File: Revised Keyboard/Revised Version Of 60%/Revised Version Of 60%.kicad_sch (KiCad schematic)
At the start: 104 parts, among them J1 AVR-ISP-6, SW1 SW_Push, U1 AT90USB1286-A, U2 PRTR5V0U2X, Y1 Crystal_GND24_Small

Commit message: Updated PCB
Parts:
- removed R1, R2: 22, Resistor_SMD:R_0805_2012Metric_Pad1.20x1.40mm_HandSolder, symbol Device:R_Small
- MX_CAPS1: footprint MX_Alps_Hybrid:MX-1U-NoLED -> MX_Alps_Hybrid:MX-1.25U-NoLED
- renumbered D1 to D_?1, D2 to D_Enter1, MX_1 to MX_?1
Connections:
- net D+: now also U1.5 (D+); no longer U2.4 (VCC)
- net D-: now also U1.4 (D-)
- net GND: now also U2.1 (GND); no longer U2.3 (IO2)
- net VCC: now also U2.4 (VCC); no longer U2.2 (IO1)
- net DN: now reaches R7.1, USB1.5 (DN2), USB1.7 (DN1)
- net DN: now also U2.3 (IO2); no longer U2.1 (GND)
- net DP: now reaches R8.2, USB1.6 (DP1), USB1.8 (DP2)
- net DP: now also U2.2 (IO1)
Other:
- moved on the sheet: U2

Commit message: Update
General Update of files
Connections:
- net MISO: now also U1.45 (PA6); no longer U1.49 (PA2)
- net MOSI: now also U1.46 (PA5); no longer U1.50 (PA1)
- net SCK: now also U1.47 (PA4); no longer U1.51 (PA0)
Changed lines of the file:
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@@
-    (stroke (width 0) (type default) (color 0 0 0 0))
-  )
-  (wire (pts (xy 121.92 58.42) (xy 128.27 58.42))
     (stroke (width 0) (type default) (color 0 0 0 0))
   )
@@
     (stroke (width 0) (type default) (color 0 0 0 0))
   )
-  (wire (pts (xy 121.92 55.88) (xy 128.27 55.88))
-    (stroke (width 0) (type default) (color 0 0 0 0))
-  )
   (wire (pts (xy 233.68 85.09) (xy 240.03 85.09))
     (stroke (width 0) (type default) (color 0 0 0 0))
@@
     (stroke (width 0) (type default) (color 0 0 0 0))
   )
-  (wire (pts (xy 121.92 53.34) (xy 128.27 53.34))
-    (stroke (width 0) (type default) (color 0 0 0 0))
-  )
   (wire (pts (xy 252.73 90.17) (xy 254 90.17))
     (stroke (width 0) (type default) (color 0 0 0 0))
@@
     (stroke (width 0) (type default) (color 0 0 0 0))
   )
-  (global_label "MOSI" (shape input) (at 128.27 55.88 0) (fields_autoplaced)
+  (global_label "MOSI" (shape input) (at 121.92 66.04 0) (fields_autoplaced)
     (effects (font (size 1.27 1.27)) (justify left))
-    (property "Intersheet References" "${INTERSHEET_REFS}" (id 0) (at 135.2793 55.9594 0)
+    (property "Intersheet References" "${INTERSHEET_REFS}" (id 0) (at 128.9293 66.1194 0)
       (effects (font (size 1.27 1.27)) (justify left) hide)
     )
@@
     )
   )
-  (global_label "SCK" (shape input) (at 128.27 53.34 0) (fields_autoplaced)
+  (global_label "SCK" (shape input) (at 121.92 63.5 0) (fields_autoplaced)
     (effects (font (size 1.27 1.27)) (justify left))
-    (property "Intersheet References" "${INTERSHEET_REFS}" (id 0) (at 134.4326 53.4194 0)
+    (property "Intersheet References" "${INTERSHEET_REFS}" (id 0) (at 128.0826 63.5794 0)
       (effects (font (size 1.27 1.27)) (justify left) hide)
     )
@@
     )
   )
-  (global_label "MISO" (shape input) (at 128.27 58.42 0) (fields_autoplaced)
+  (global_label "MISO" (shape input) (at 121.92 68.58 0) (fields_autoplaced)
     (effects (font (size 1.27 1.27)) (justify left))
-    (property "Intersheet References" "${INTERSHEET_REFS}" (id 0) (at 135.2793 58.4994 0)
+    (property "Intersheet References" "${INTERSHEET_REFS}" (id 0) (at 128.9293 68.6594 0)
       (effects (font (size 1.27 1.27)) (justify left) hide)
     )

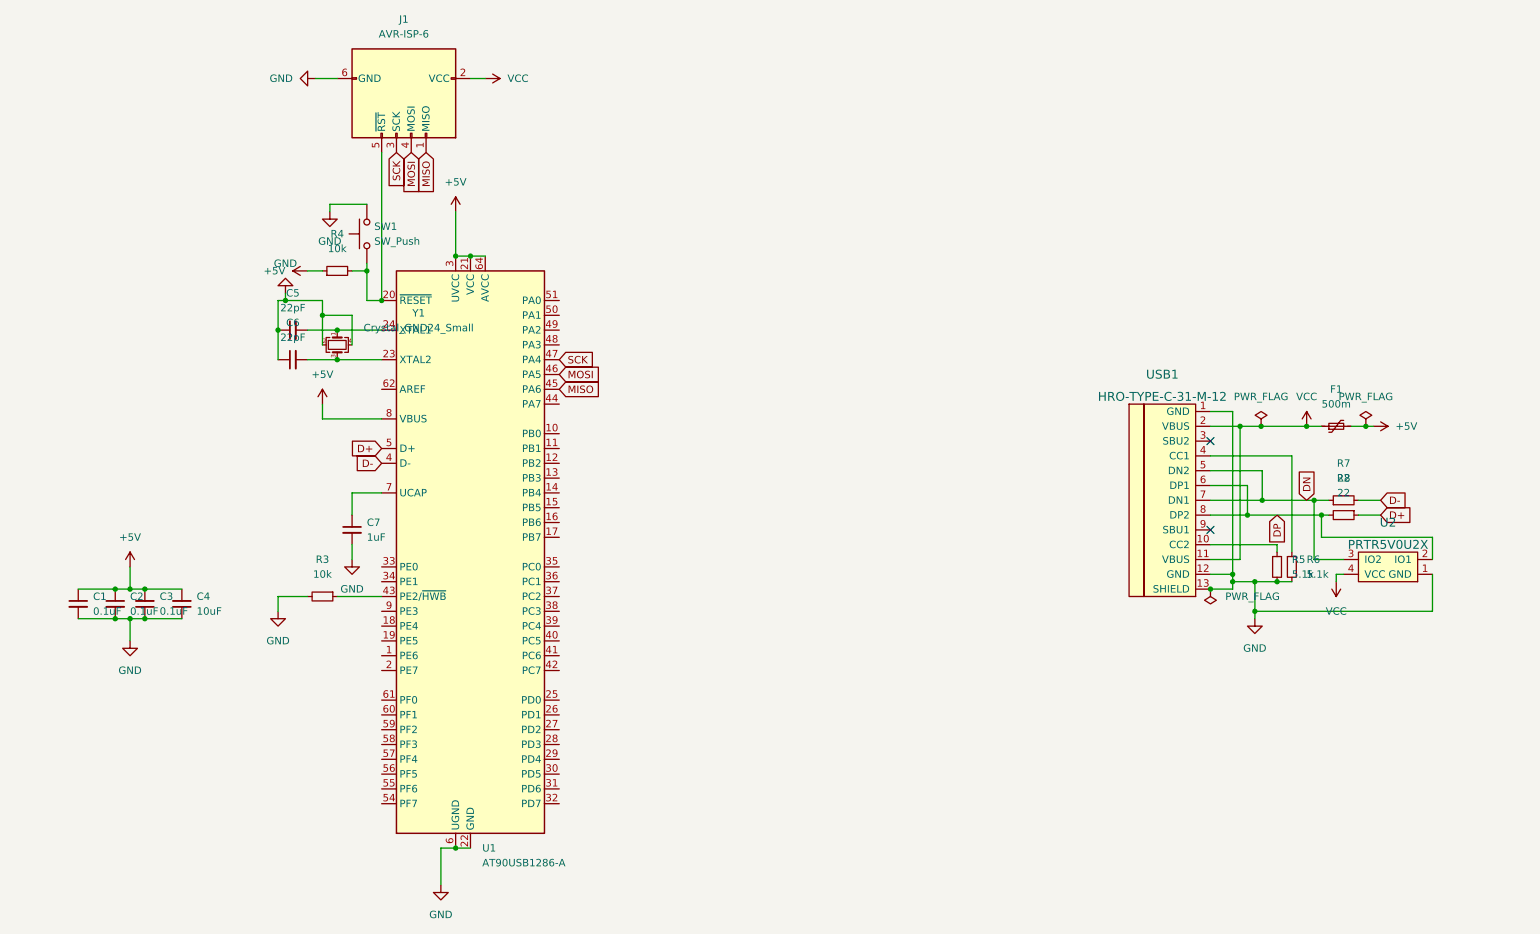
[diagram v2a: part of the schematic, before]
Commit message: Keyboard Update
Changed to a smaller microcontroller
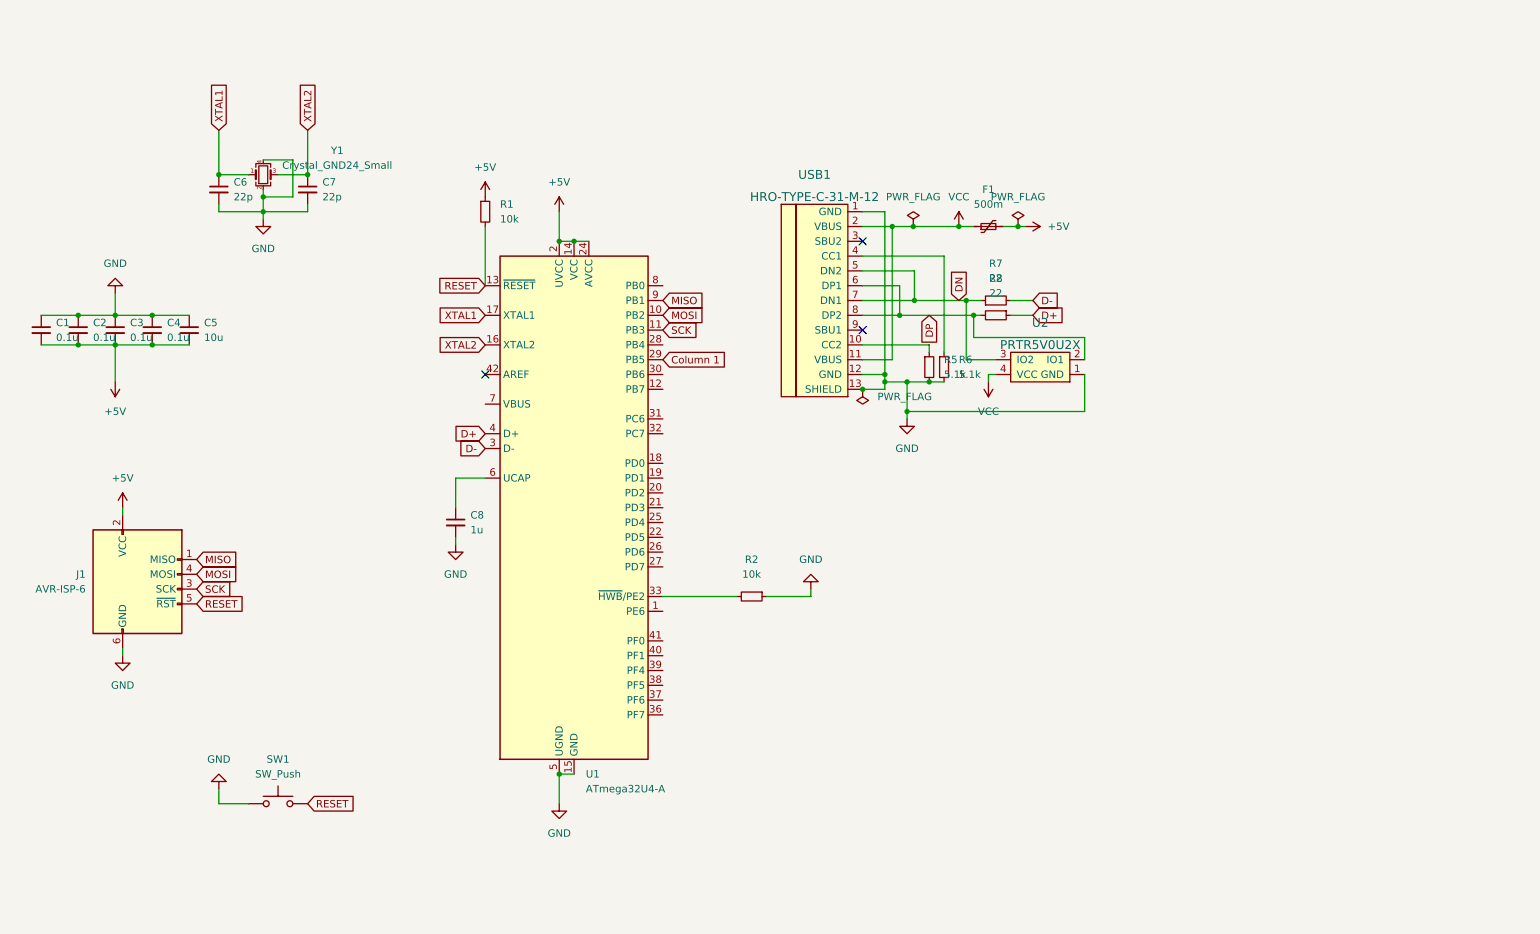
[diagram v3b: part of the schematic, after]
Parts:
- removed R3, R4: 10k, Resistor_SMD:R_0805_2012Metric_Pad1.20x1.40mm_HandSolder, symbol Device:R_Small
- removed U1: AT90USB1286-A, Package_QFP:TQFP-64_14x14mm_P0.8mm, symbol MCU_Microchip_AVR:AT90USB1286-A
- added C8: 1u, Capacitor_SMD:C_0805_2012Metric, symbol Device:C_Small
- added R1, R2: 10k, Resistor_SMD:R_0805_2012Metric_Pad1.20x1.40mm_HandSolder, symbol Device:R_Small
- added U1: ATmega32U4-A, Package_QFP:TQFP-44_10x10mm_P0.8mm, symbol MCU_Microchip_ATmega:ATmega32U4-A
- C1, C2, C3: value 0.1uF -> 0.1u
- C4: value 10uF -> 0.1u
- C5: value 22pF -> 10u
- C6: value 22pF -> 22p
- C7: value 1uF -> 22p
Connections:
- net +5V: now also C1.2, C2.2, C5.2, J1.2 (VCC), R1.1, U1.14 (VCC), U1.2 (UVCC), U1.24 (AVCC), U1.34 (VCC), U1.44 (AVCC); no longer C1.1, C2.1
- net D+: now also U1.4 (D+)
- net D-: now also U1.3 (D-)
- net GND: now also C1.1, C2.1, C6.2, SW1.1, C8.2, R2.1, U1.15 (GND), U1.23 (GND), U1.35 (GND), U1.43 (GND), U1.5 (UGND); no longer C1.2, C2.2, C6.1, SW1.2
- net MISO: now also U1.9 (PB1)
- net MOSI: now also U1.10 (PB2)
- net SCK: now also U1.11 (PB3)
- net VCC: no longer J1.2 (VCC)
- net XTAL2: now reaches C7.1
- net XTAL2: now also Y1.3, U1.16 (XTAL2)
- net RESET: now reaches J1.5 (~{RST})
- net RESET: now also SW1.2, R1.2, U1.13 (~{RESET}); no longer SW1.1
- net XTAL1: now reaches Y1.1
- net XTAL1: now also C6.1, U1.17 (XTAL1); no longer C5.2
- new net: R2.2, U1.33 (~{HWB}/PE2)
- new net: C8.1, U1.6 (UCAP)
- new net Column 1: U1.29 (PB5)
- no-connect marks 2 -> 3
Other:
- moved on the sheet: F1, R5, R6, R7, R8, U2, USB1

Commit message: Keyboard Nearly finished
All components wired up on the PCB
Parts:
- removed J1: AVR-ISP-6, random-keyboard-parts:Reset_Pretty-Mask, symbol Connector:AVR-ISP-6
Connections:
- net MOSI is gone; now on net Column 6: U1.10 (PB2)
- net SCK is gone; now on net Column 7: U1.11 (PB3)
- net +5V: now also U1.7 (VBUS)
- net Column 1: now also MX_CTRL1.1 (COL), MX_ESC1.1 (COL), MX_SHIFT1.1 (COL), MX_TAB1.1 (COL), U1.37 (PF6); no longer U1.29 (PB5)
- net Row 1: now reaches D_BACKSPACE1.1 (K), D_E1.1 (K), D_ESC1.1 (K), D_I1.1 (K), D_O1.1 (K), D_P1.1 (K), D_Q1.1 (K), D_R1.1 (K), D_T1.1 (K), D_U1.1 (K), D_W1.1 (K), D_Y1.1 (K)
- net Row 1: now also U1.32 (PC7)
- net Row 2: now reaches D_?1.1 (K), D_A1.1 (K), D_D1.1 (K), D_Enter1.1 (K), D_F1.1 (K), D_G1.1 (K), D_H1.1 (K), D_J1.1 (K), D_K1.1 (K), D_L1.1 (K), D_S1.1 (K), D_TAB1.1 (K)
- net Row 2: now also U1.31 (PC6)
- net Column 3: now reaches MX_ALT1.1 (COL), MX_S1.1 (COL), MX_W1.1 (COL), MX_X1.1 (COL)
- net Column 3: now also U1.39 (PF4)
- net Column 10: now reaches MX_)1.1 (COL), MX_FN1.1 (COL), MX_L1.1 (COL), MX_O1.1 (COL)
- net Column 10: now also U1.20 (PD2)
- net Row 4: now reaches D_ALT1.1 (K), D_CAPS1.1 (K), D_CTRL1.1 (K), D_FN1.1 (K), D_SPACEBAR1.1 (K), D_SUPER1.1 (K)
- net Row 4: now also U1.29 (PB5)
- net Column 6: now reaches MX_B1.1 (COL), MX_G1.1 (COL), MX_T1.1 (COL)
- net Column 9: now reaches MX_(1.1 (COL), MX_I1.1 (COL), MX_K1.1 (COL)
- net Column 9: now also U1.19 (PD1)
- net Row 3: now reaches D_(1.1 (K), D_)1.1 (K), D_B1.1 (K), D_C1.1 (K), D_M1.1 (K), D_N1.1 (K), D_RSHIFT1.1 (K), D_SHIFT1.1 (K), D_V1.1 (K), D_X1.1 (K), D_Z1.1 (K)
- net Row 3: now also U1.30 (PB6)
- net Column 11: now reaches MX_?1.1 (COL), MX_CAPS1.1 (COL), MX_P1.1 (COL), MX_RSHIFT1.1 (COL)
- net Column 11: now also U1.21 (PD3)
- net Column 12: now reaches MX_BACKSPACE1.1 (COL), MX_ENTER1.1 (COL)
- net Column 12: now also U1.22 (PD5)
- net Column 8: now reaches MX_J1.1 (COL), MX_M1.1 (COL), MX_U1.1 (COL)
- net Column 8: now also U1.12 (PB7)
- net Column 4: now reaches MX_C1.1 (COL), MX_D1.1 (COL), MX_E1.1 (COL)
- net Column 4: now also U1.40 (PF1)
- net Column 2: now reaches MX_A1.1 (COL), MX_Q1.1 (COL), MX_SUPER1.1 (COL), MX_Z1.1 (COL)
- net Column 2: now also U1.38 (PF5)
- net Column 7: now reaches MX_H1.1 (COL), MX_N1.1 (COL), MX_SPACEBAR1.1 (COL), MX_Y1.1 (COL)
- net Column 5: now reaches MX_F1.1 (COL), MX_R1.1 (COL), MX_V1.1 (COL)
- net Column 5: now also U1.41 (PF0)
- net MISO: no longer names the net of U1.9 (PB1)
